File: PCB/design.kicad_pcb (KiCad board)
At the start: 4 copper layers, 78.7 x 38.5 mm, 64 parts, among them IC3 W5100S-L, J1 BNC, J2 BNC, J3 2250056-1, U1 MCP6002-xMC, U2 MCP6002-xMC, U3 NUCLEO-L432KC, Y2 25M

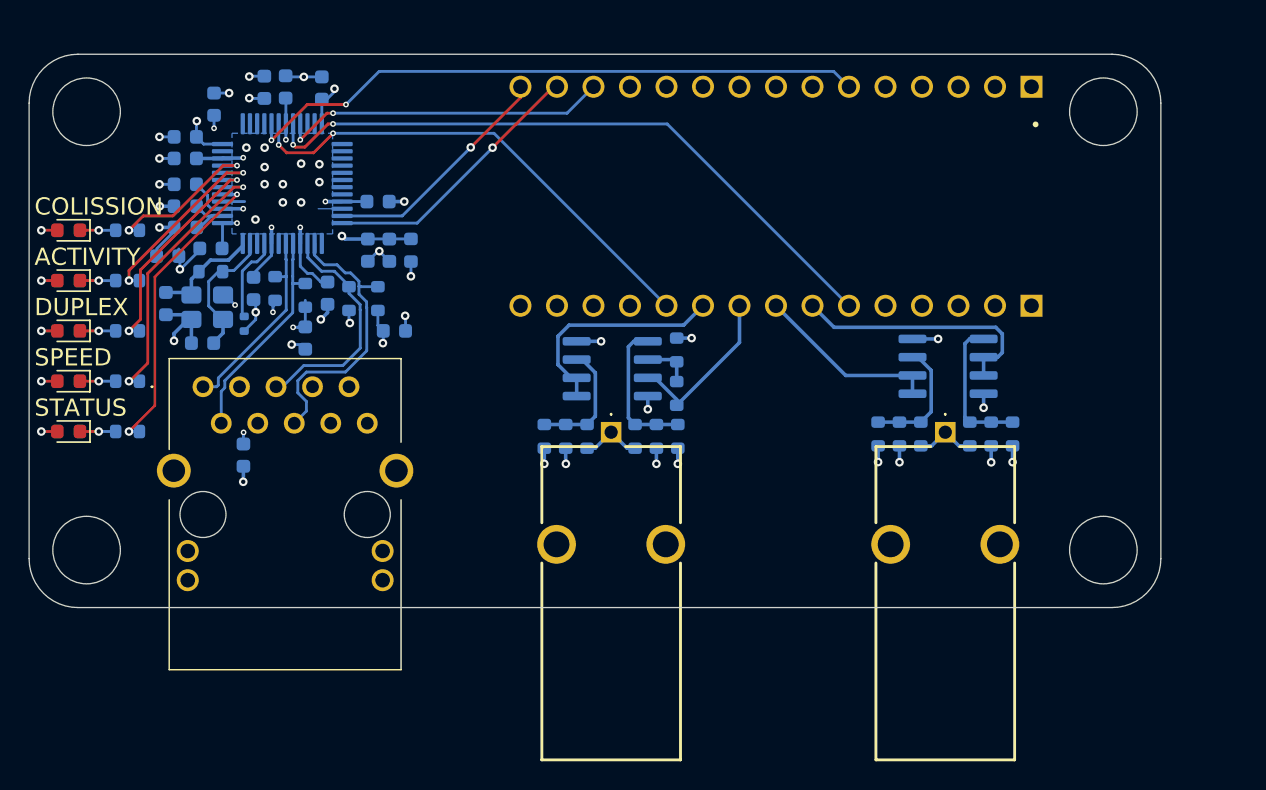
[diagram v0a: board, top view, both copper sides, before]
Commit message: lock board edge
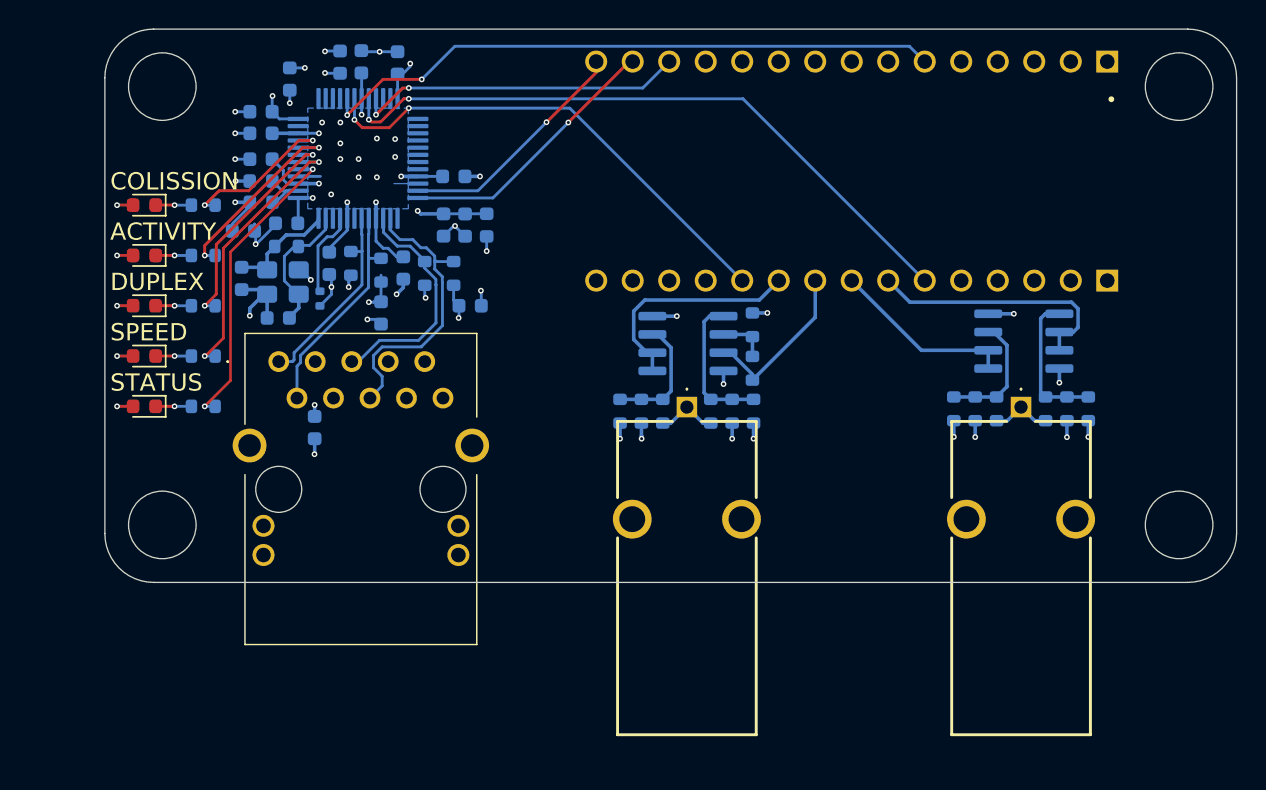
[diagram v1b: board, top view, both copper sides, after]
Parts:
- moved C1 5.55 mm to (136.4, 79.1)
- moved C14 5.55 mm to (140.3, 87.0)
- moved C18 5.55 mm to (135.2, 96.5)
- moved C3 5.55 mm to (128.9, 80.2)
- moved C4 5.55 mm to (132.4, 79.0)
- moved C5 5.55 mm to (141.1, 90.4)
- moved C6 5.55 mm to (131.6, 93.0)
- moved C8 5.55 mm to (128.7, 90.3)
- moved C9 5.55 mm to (139.6, 90.4)
- moved FB1 5.55 mm to (142.6, 90.4)
- moved G1 5.55 mm to (190.8, 111.2)
- moved G3 5.55 mm to (190.8, 80.8)
- moved IC3 5.55 mm to (133.6, 85.8)
- moved J1 5.55 mm to (156.5, 103.0)
- moved J2 5.55 mm to (179.8, 103.0)
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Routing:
- net /wiznet/3V3A: track 41.4 -> 42.0 mm
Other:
- board size 78.7 x 38.5 mm -> 78.8 x 38.5 mm

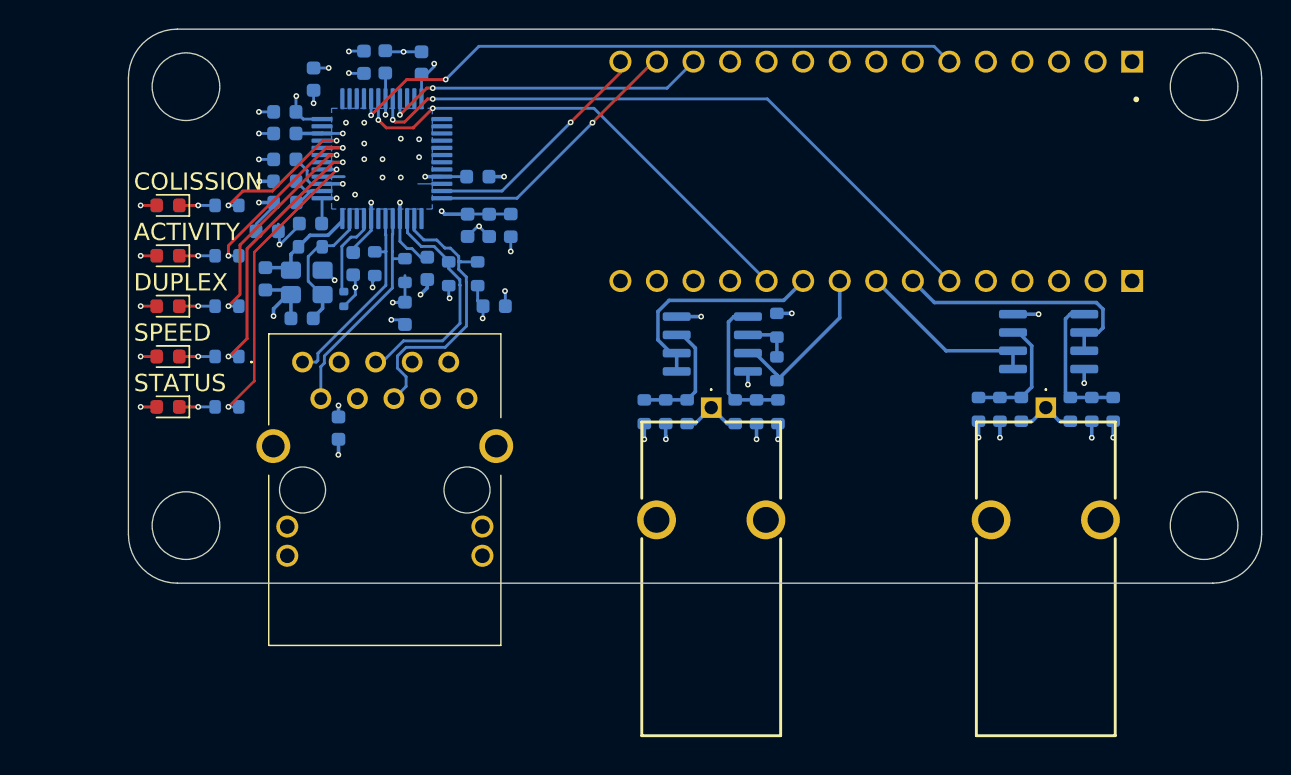
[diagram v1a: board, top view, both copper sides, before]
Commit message: add better ground vias; rename footprints and 3d-models
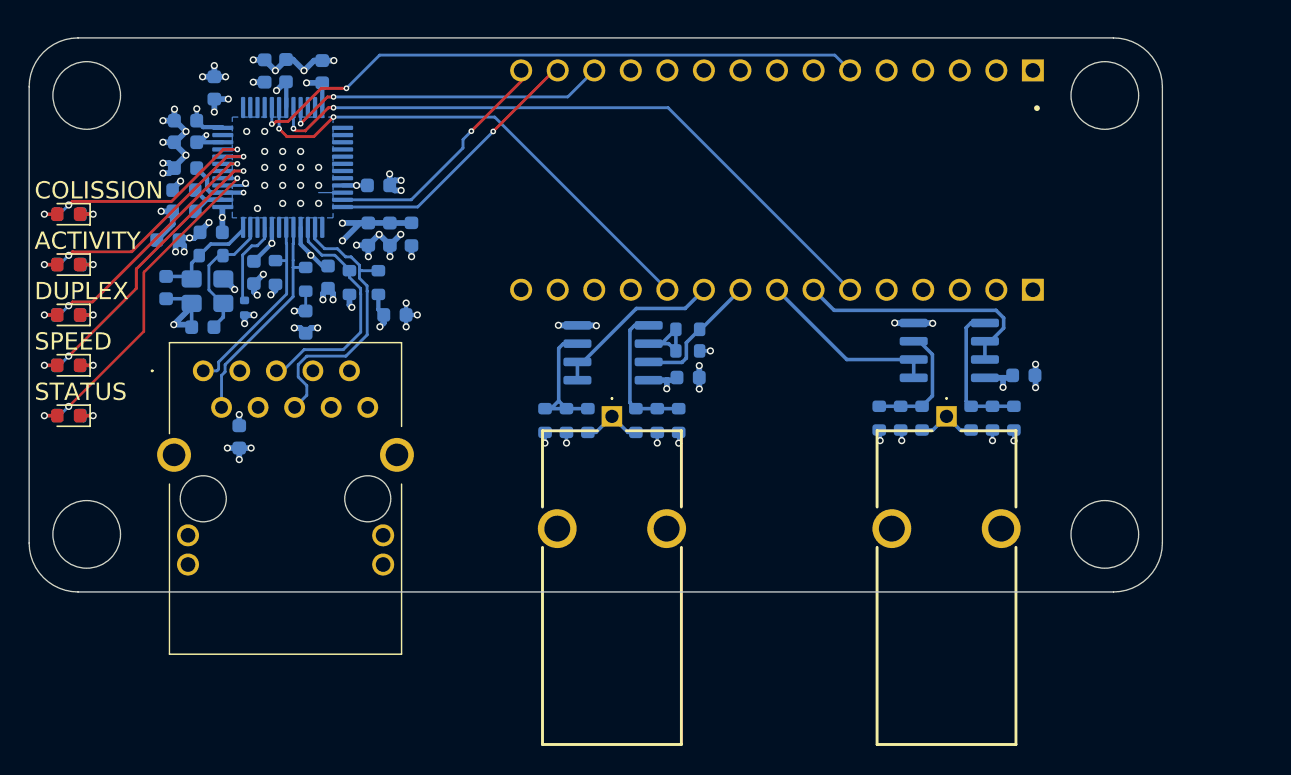
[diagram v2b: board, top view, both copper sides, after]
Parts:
- added C20: 0.1u, Capacitor_SMD:C_0603_1608Metric, B.Cu at (178.2, 100.8)
- added C21: 0.1u, Capacitor_SMD:C_0603_1608Metric, B.Cu at (154.9, 101.0)
- G1, G2, G3, G4: footprint customLib:rubber-feet -> customLib:G2009
- moved R17 11.0 mm to (111.9, 100.1), turned to 180 degrees
- moved R18 11.0 mm to (111.9, 96.6), turned to 180 degrees
- moved R16 11.0 mm to (111.9, 103.6), turned to 180 degrees
- moved R19 11.0 mm to (111.9, 93.1), turned to 180 degrees
- moved R20 11.0 mm to (111.9, 89.6), turned to 180 degrees
- moved FB2 7.04 mm to (119.9, 89.4)
- moved FB3 7.04 mm to (119.9, 87.9)
- moved C9 6.93 mm to (132.7, 91.0)
- moved C1 6.93 mm to (129.5, 79.7)
- moved C14 6.93 mm to (133.4, 87.6)
- moved C18 6.93 mm to (128.3, 97.1)
- moved C3 6.93 mm to (122.0, 80.8)
- moved C4 6.93 mm to (125.5, 79.7)
- moved C5 6.93 mm to (134.2, 91.0)
- moved C6 6.93 mm to (124.7, 93.7)
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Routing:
- net GND: track 41.4 -> 67.1 mm, vias 34 -> 73
- net /wiznet/COLN: track 11.2 -> 15.5 mm
- net /wiznet/ACTn: track 13.6 -> 17.4 mm
- net /wiznet/1V2D: track 37.6 -> 41.4 mm, vias 6 -> 7
- net /CH0_10: track 15.9 -> 12.1 mm
- net /CH0_1: track 11.8 -> 9.12 mm
- net Net-(U1B--): track 3.45 -> 5.91 mm
- net /wiznet/DPXn: track 15.7 -> 18.0 mm
- net /wiznet/3V3A: track 42.0 -> 43.8 mm, vias 4 -> 5
- net Net-(U1A-+): track 8.49 -> 10.00 mm
- net /wiznet/LNKn: track 21.4 -> 22.9 mm
- net /wiznet/SPDn: track 19.3 -> 20.7 mm
- net /wiznet/1V2A: track 18.4 -> 19.3 mm
- net Net-(D5-K): track 2.50 -> 1.76 mm
- net Net-(D4-K): track 2.50 -> 1.76 mm
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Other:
- board size 78.8 x 38.5 mm -> 78.7 x 38.5 mm

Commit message: remove unneeded pin; update invalid footprint
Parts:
- U3: footprint customLib:MODULE_NUCLEO-L432KC -> customLib:NUCLEO-L432KC
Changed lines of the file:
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@@
 	(net 76 "/CH1_36")
 	(net 77 "/CH1_10")
-	(footprint "customLib:MODULE_NUCLEO-L432KC"
+	(footprint "customLib:NUCLEO-L432KC"
 		(layer "F.Cu")
 		(at 162.6365 87.24 -90)
 		(property "Reference" "U3"
-			(at -5.715 -26.035 90)
+			(at -7.5 -19.5 270)
 			(layer "F.SilkS")
 			(hide yes)
@@
 		)
 		(property "Value" "NUCLEO-L432KC"
-			(at 3.81 26.035 90)
+			(at 3.81 26.035 270)
 			(layer "F.Fab")
 			(hide yes)
@@
 		)
 		(property "Datasheet" ""
-			(at 0 0 90)
+			(at 0 0 270)
 			(layer "F.Fab")
 			(hide yes)
@@
 		)
 		(property "Description" ""
-			(at 0 0 90)
+			(at 0 0 270)
 			(layer "F.Fab")
 			(hide yes)
@@
 			(layer "F.Fab")
 		)
-		(fp_text user "${REFERENCE}"
-			(at 5.519 8.865 0)
-			(layer "F.Fab")
-			(effects
-				(font
-					(size 1.27 1.27)
-					(thickness 0.254)
-				)
-			)
-		)
 		(pad "" np_thru_hole circle
 			(at 0 8.89)
@@
 			(layer "F.Fab")
 		)
-		(fp_text user "${REFERENCE}"
-			(at 0 11.042 0)
-			(layer "F.Fab")
-			(effects
-				(font
-					(size 1.27 1.27)
-					(thickness 0.254)
-				)
-			)
-		)
 		(pad "1" thru_hole rect
 			(at 0 0)
@@
 			(layer "F.Fab")
 		)
-		(fp_text user "${REFERENCE}"
-			(at 0 11.042 0)
-			(layer "F.Fab")
-			(effects
-				(font
-					(size 1.27 1.27)
-					(thickness 0.254)
-				)
-			)
-		)
 		(pad "1" thru_hole rect
 			(at 0 0)
@@
 			(keep_text_aligned yes)
 		)
-		(gr_text "78.7500 mm"
+		(gr_text "78,7500 mm"
 			(at 148.4765 73.21 0)
 			(layer "Dwgs.User")
@@
 			(keep_text_aligned yes)
 		)
-		(gr_text "38.5000 mm"
+		(gr_text "38,5000 mm"
 			(at 189.7015 96.61 90)
 			(layer "Dwgs.User")

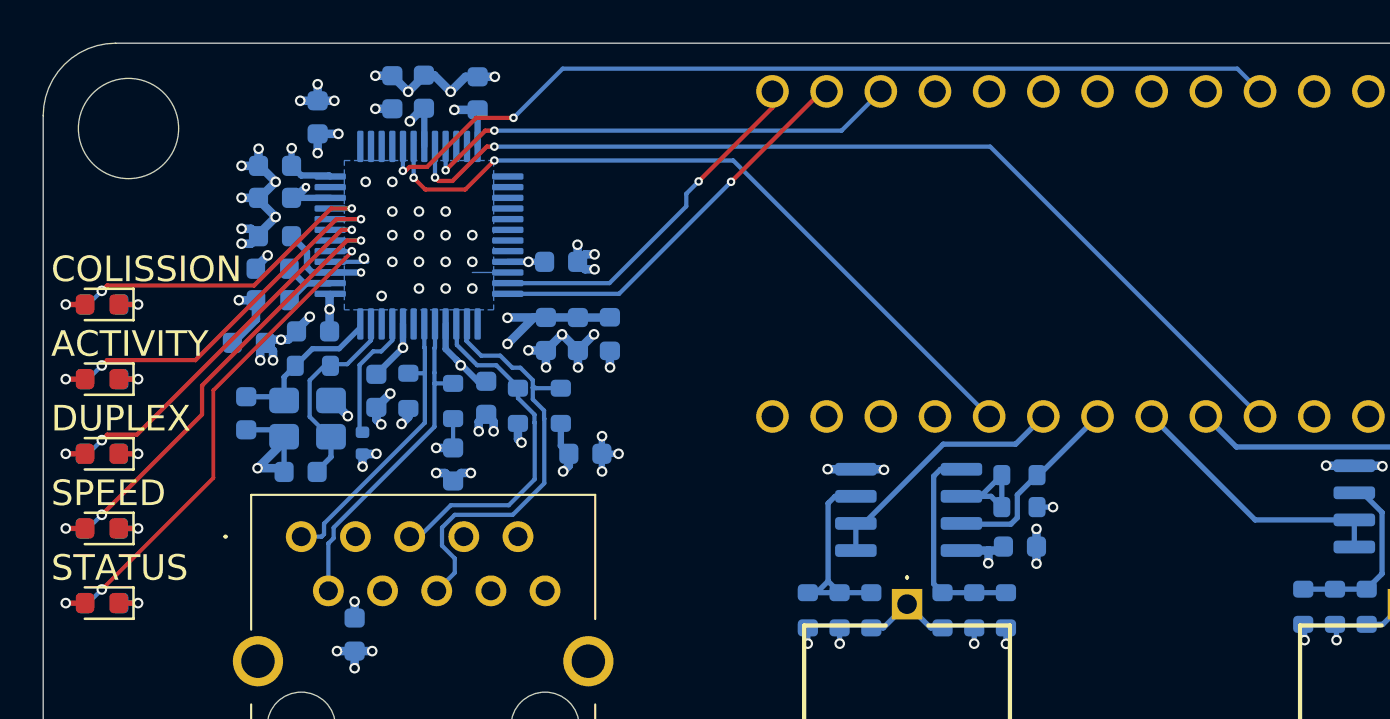
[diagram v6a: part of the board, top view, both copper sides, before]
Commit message: make vias bigger than 0.3mm/0.45mm
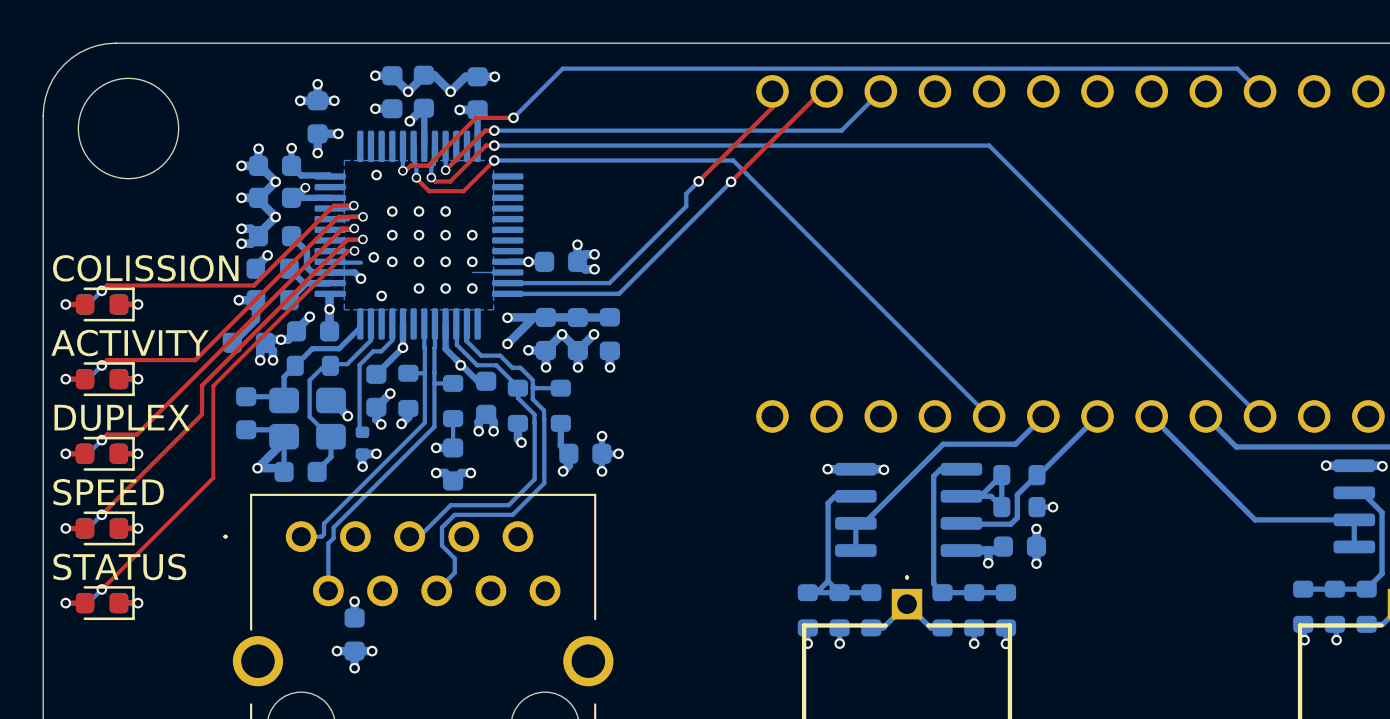
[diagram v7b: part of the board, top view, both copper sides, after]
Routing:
- net GND: track 67.1 -> 66.8 mm, vias 73 -> 72

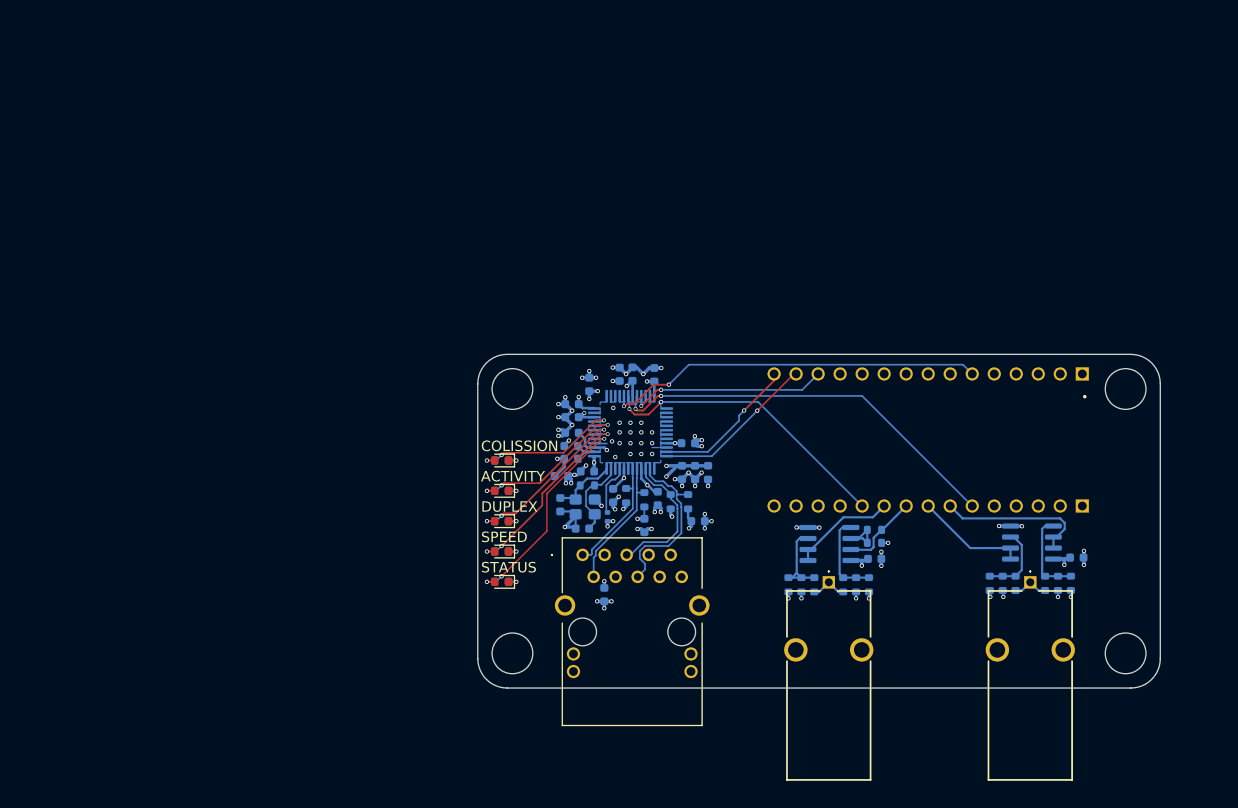
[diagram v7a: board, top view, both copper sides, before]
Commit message: add V1.0 silkscreen text
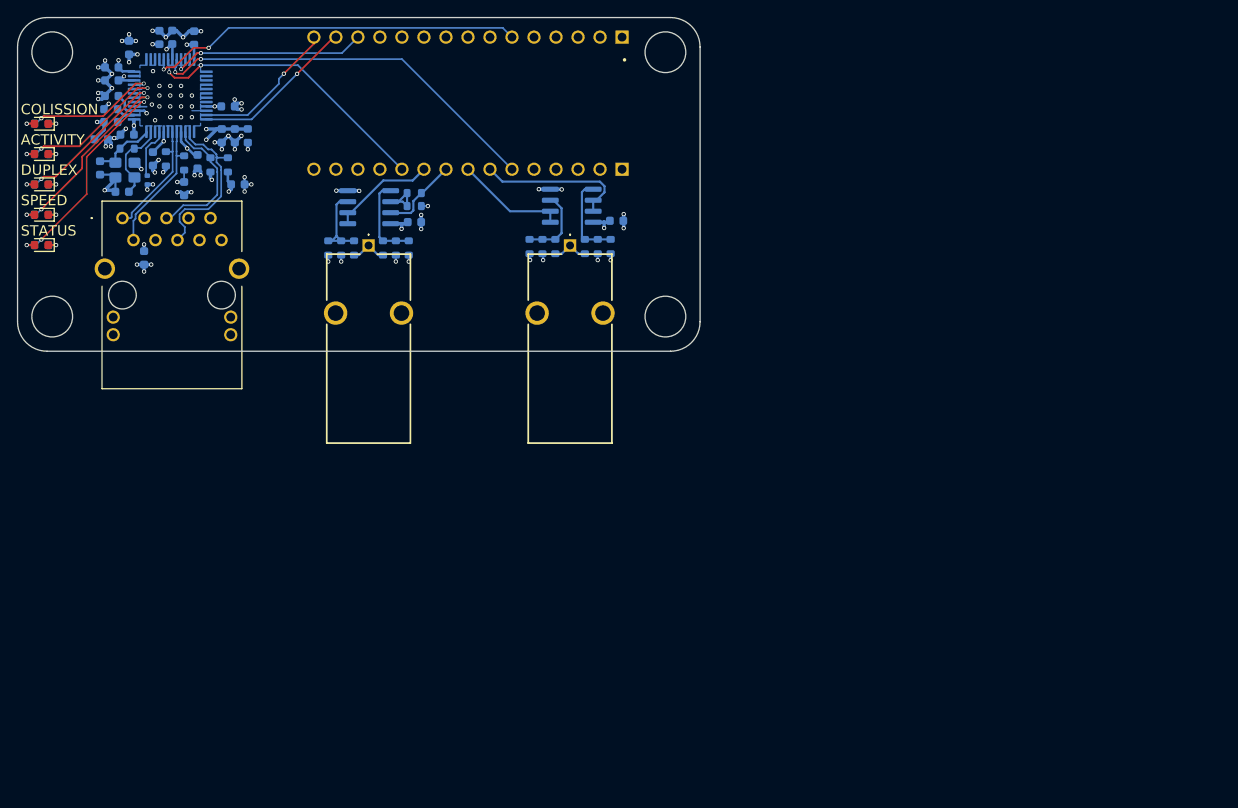
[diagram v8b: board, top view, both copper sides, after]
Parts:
- moved C12 65.8 mm to (73.8, 40.8)
- moved C17 65.8 mm to (81.4, 57.8)
- moved C21 65.8 mm to (101.8, 62.1)
- moved J3 65.8 mm to (68.1, 61.6)
- moved R11 65.8 mm to (122.9, 64.9)
- moved R2 65.8 mm to (98.2, 65.1)
- moved R21 65.8 mm to (68.6, 53.6)
- moved R23 65.8 mm to (78.3, 55.5)
- moved R6 65.8 mm to (91.8, 65.1)
- moved U2 65.8 mm to (119.9, 60.2)
- moved U3 65.8 mm to (109.5, 48.4)
- moved C1 65.8 mm to (76.4, 40.9)
- moved C10 65.8 mm to (66.9, 45.8)
- moved C11 65.8 mm to (65.6, 52.5)
- moved C13 65.8 mm to (76.8, 55.1)
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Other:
- board size 78.7 x 38.5 mm -> 78.8 x 38.5 mm
- board text added: "V1.0"
